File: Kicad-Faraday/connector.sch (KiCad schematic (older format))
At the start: 29 parts, among them P11 DNP, P12 DNP, P13 DNP, P14 DNP, P3 DNP, P4 DNP, P6 DNP, P7 DNP, P8 DNP, P9 DNP

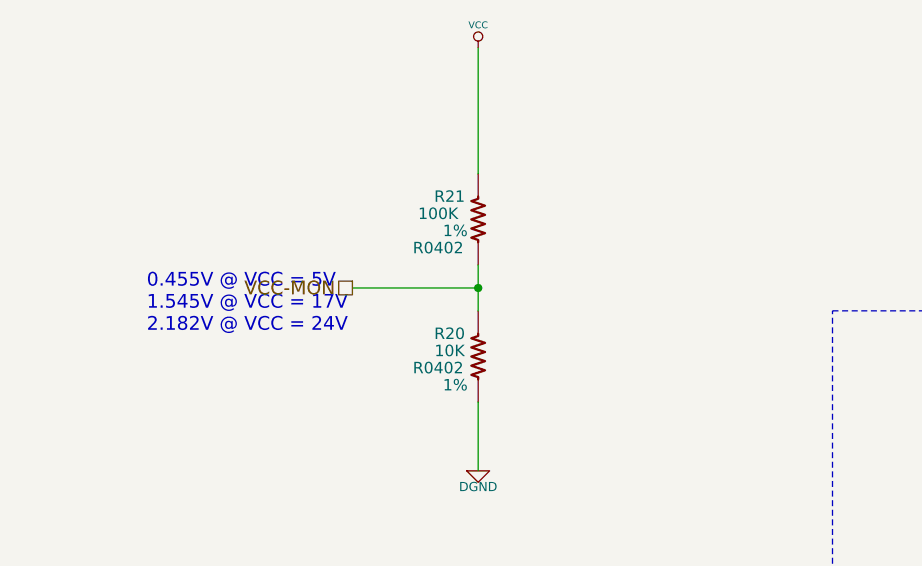
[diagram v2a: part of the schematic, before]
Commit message: Updated with ideal diode after realizing that the normal diodes have too large of a voltage drop... woops. Also added via fences back in.
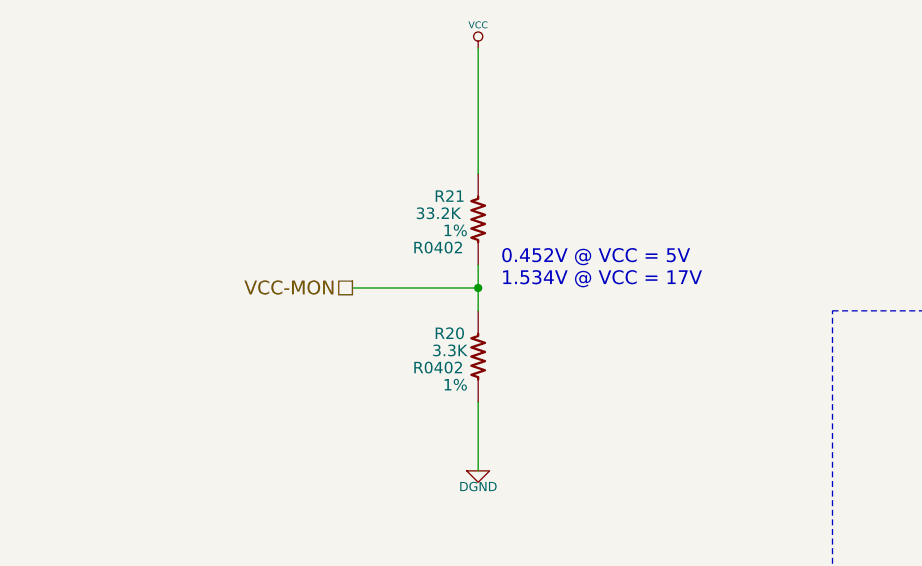
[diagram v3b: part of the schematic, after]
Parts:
- R20: value 10K -> 3.3K
- R21: value 100K -> 33.2K
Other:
- note added: "0.452V @ VCC = 5V\n1.534V @ VCC = 17V"
- note removed: "0.455V @ VCC = 5V\n1.545V @ VCC = 17V\n2.182V @ VCC = 24V"
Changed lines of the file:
@@
 Sheet 10 11
 Title "Faraday Wireless Node"
-Date "11 nov 2016"
+Date "13 nov 2016"
 Rev "C"
 Comp "FaradayRF"
@@
 Mounting Holes 125 mil
 $Comp
-L +3.3V #PWR090
+L +3.3V #PWR091
 U 1 1 54FD3F6B
 P 6000 5000
-F 0 "#PWR090" H 6000 4960 30  0001 C CNN
+F 0 "#PWR091" H 6000 4960 30  0001 C CNN
 F 1 "+3.3V" H 6000 5110 30  0000 C CNN
 F 2 "" H 6000 5000 60  0000 C CNN
@@
 $EndComp
 $Comp
-L VCC #PWR091
+L VCC #PWR092
 U 1 1 54FE705E
 P 6450 8900
-F 0 "#PWR091" H 6450 9000 30  0001 C CNN
+F 0 "#PWR092" H 6450 9000 30  0001 C CNN
 F 1 "VCC" H 6450 9000 30  0000 C CNN
 F 2 "" H 6450 8900 60  0000 C CNN
@@
 Ext. Power/MOSFET
 $Comp
-L DGND #PWR092
+L DGND #PWR093
 U 1 1 55A56688
 P 11550 3900
-F 0 "#PWR092" H 11550 3900 40  0001 C CNN
+F 0 "#PWR093" H 11550 3900 40  0001 C CNN
 F 1 "DGND" H 11550 3830 40  0000 C CNN
 F 2 "~" H 11550 3900 60  0000 C CNN
@@
 $EndComp
 $Comp
-L DGND #PWR093
+L DGND #PWR094
 U 1 1 55A56A07
 P 6200 4600
-F 0 "#PWR093" H 6200 4600 40  0001 C CNN
+F 0 "#PWR094" H 6200 4600 40  0001 C CNN
 F 1 "DGND" H 6200 4530 40  0000 C CNN
 F 2 "~" H 6200 4600 60  0000 C CNN
@@
 $EndComp
 $Comp
-L GNDPWR #PWR094
+L GNDPWR #PWR095
 U 1 1 55C2A828
 P 5750 7150
-F 0 "#PWR094" H 5750 7200 40  0001 C CNN
+F 0 "#PWR095" H 5750 7200 40  0001 C CNN
 F 1 "GNDPWR" H 5750 7070 40  0000 C CNN
 F 2 "" H 5750 7150 60  0000 C CNN
@@
 P 3050 2500
 F 0 "R21" H 2925 2600 50  0000 C CNN
-F 1 "100K" H 2875 2525 50  0000 C CNN
+F 1 "33.2K" H 2875 2525 50  0000 C CNN
 F 2 "R0402" H 2875 2375 50  0000 C CNN
 F 3 "" H 3050 2500 60  0000 C CNN
@@
 P 3050 3100
 F 0 "R20" H 2925 3200 50  0000 C CNN
-F 1 "10K" H 2925 3125 50  0000 C CNN
+F 1 "3.3K" H 2925 3125 50  0000 C CNN
 F 2 "R0402" H 2875 3050 50  0000 C CNN
 F 3 "" H 3050 3100 60  0000 C CNN
@@
 Text HLabel 2500 2800 0    60   UnSpc ~ 0
 VCC-MON
-Text Notes 1600 3000 0    60   ~ 0
-0.455V @ VCC = 5V\n1.545V @ VCC = 17V\n2.182V @ VCC = 24V
-$Comp
-L DGND #PWR095
+Text Notes 3150 2800 0    60   ~ 0
+0.452V @ VCC = 5V\n1.534V @ VCC = 17V
+$Comp
+L DGND #PWR096
 U 1 1 55DDCB2D
 P 3050 3600
-F 0 "#PWR095" H 3050 3600 40  0001 C CNN
+F 0 "#PWR096" H 3050 3600 40  0001 C CNN
 F 1 "DGND" H 3050 3530 40  0000 C CNN
 F 2 "~" H 3050 3600 60  0000 C CNN
@@
 	2100 9300 2700 9300
 $Comp
-L PWR_FLAG #FLG096
+L PWR_FLAG #FLG097
 U 1 1 578D1476
 P 6625 9550
-F 0 "#FLG096" H 6625 9645 30  0001 C CNN
+F 0 "#FLG097" H 6625 9645 30  0001 C CNN
 F 1 "PWR_FLAG" H 6625 9730 30  0000 C CNN
 F 2 "" H 6625 9550 60  0000 C CNN
@@
 $EndComp
 $Comp
-L DGND #PWR097
+L DGND #PWR098
 U 1 1 578D1483
 P 5950 9500
-F 0 "#PWR097" H 5950 9500 40  0001 C CNN
+F 0 "#PWR098" H 5950 9500 40  0001 C CNN
 F 1 "DGND" H 5950 9430 40  0000 C CNN
 F 2 "~" H 5950 9500 60  0000 C CNN
@@
 Place on bottom of PCB
 $Comp
-L VCC #PWR098
+L VCC #PWR099
 U 1 1 578D8DFD
 P 3050 1750
-F 0 "#PWR098" H 3050 1850 30  0001 C CNN
+F 0 "#PWR099" H 3050 1850 30  0001 C CNN
 F 1 "VCC" H 3050 1850 30  0000 C CNN
 F 2 "" H 3050 1750 60  0000 C CNN
@@
 $EndComp
 $Comp
-L VCC #PWR099
+L VCC #PWR0100
 U 1 1 578D92A7
 P 6000 5400
-F 0 "#PWR099" H 6000 5500 30  0001 C CNN
+F 0 "#PWR0100" H 6000 5500 30  0001 C CNN
 F 1 "VCC" H 6000 5500 30  0000 C CNN
 F 2 "" H 6000 5400 60  0000 C CNN
@@
 $EndComp
 $Comp
-L PWR_FLAG #FLG0100
+L PWR_FLAG #FLG0101
 U 1 1 578DD49D
 P 6025 9450
-F 0 "#FLG0100" H 6025 9545 30  0001 C CNN
+F 0 "#FLG0101" H 6025 9545 30  0001 C CNN
 F 1 "PWR_FLAG" H 6025 9630 30  0000 C CNN
 F 2 "" H 6025 9450 60  0000 C CNN
@@
 $EndComp
 $Comp
-L DGND #PWR0101
+L DGND #PWR0102
 U 1 1 579B84BD
 P 7375 9600
-F 0 "#PWR0101" H 7375 9600 40  0001 C CNN
+F 0 "#PWR0102" H 7375 9600 40  0001 C CNN
 F 1 "DGND" H 7375 9530 40  0000 C CNN
 F 2 "~" H 7375 9600 60  0000 C CNN
@@
 	6450 8950 5850 8950
 $Comp
-L VCC #PWR0102
+L VCC #PWR0103
 U 1 1 579FA7FA
 P 6450 9575
-F 0 "#PWR0102" H 6450 9675 30  0001 C CNN
+F 0 "#PWR0103" H 6450 9675 30  0001 C CNN
 F 1 "VCC" H 6450 9675 30  0000 C CNN
 F 2 "" H 6450 9575 60  0000 C CNN

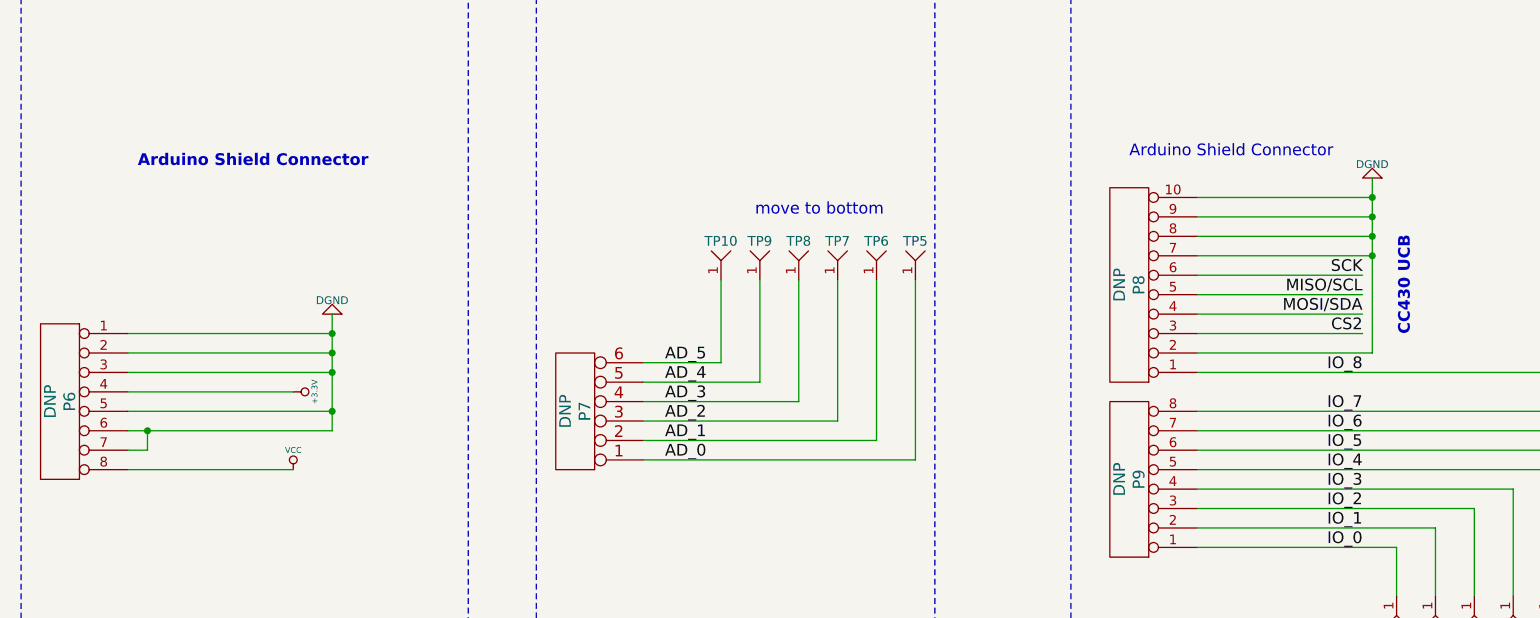
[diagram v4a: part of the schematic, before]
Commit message: Cleaned up a few connections on the schematic to make sure wire junctions were used. Also added a few notes such as LED color. Output new PDF of Schematics and updated Rev to Rev D1 for PCB:NG
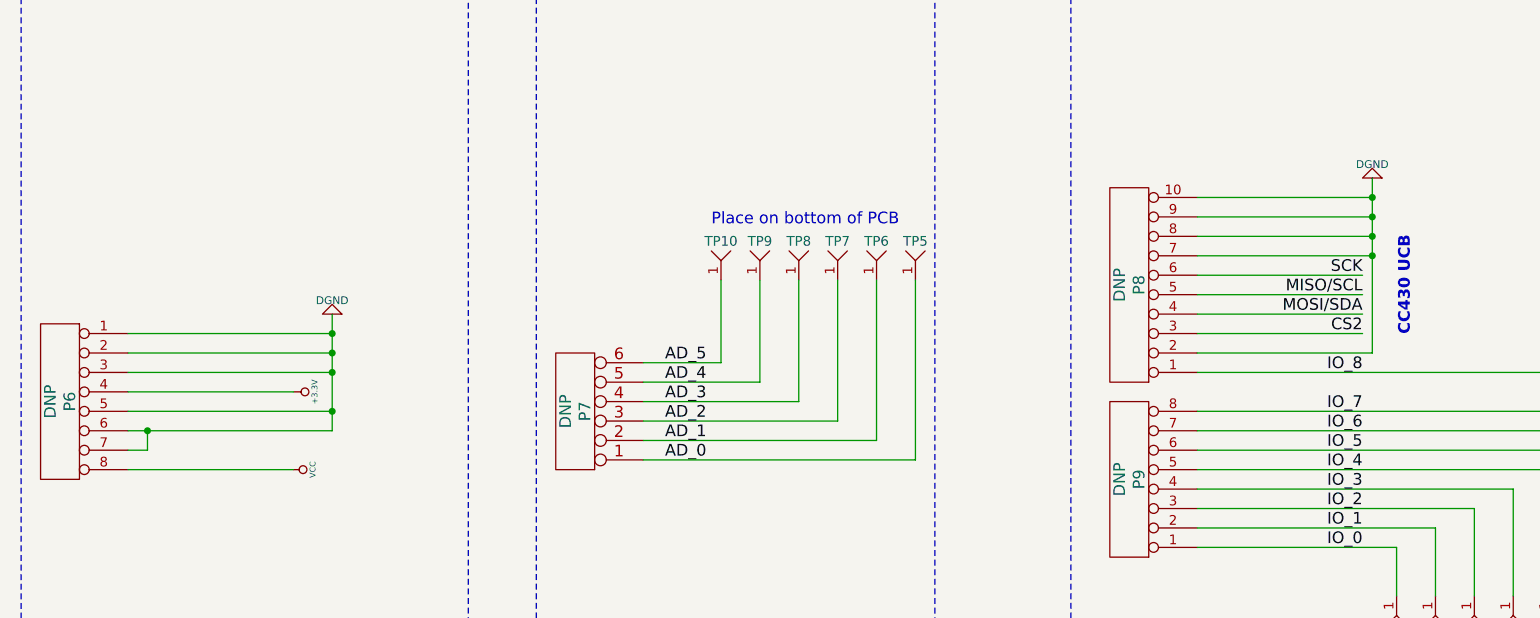
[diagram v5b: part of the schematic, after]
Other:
- note removed: "Arduino Shield Connector"
- note removed: "move to bottom"
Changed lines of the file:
@@
 Sheet 10 11
 Title "Faraday Wireless Node"
-Date "14 nov 2016"
-Rev "C"
+Date "15 nov 2016"
+Rev "D1"
 Comp "FaradayRF"
 Comment1 "www.FaradayRF.com"
@@
 Text Label 2700 9500 2    60   ~ 0
 CS2
-Text Notes 5200 3850 0    60   ~ 12
-Arduino Shield Connector
-Text Notes 10300 3800 0    60   ~ 0
-Arduino Shield Connector
 $Sheet
 S 11950 8550 950  350
@@
 Wire Wire Line
 	5850 9600 7075 9600
-Text Notes 8375 4100 0    60   ~ 0
-move to bottom
 $Comp
 L TEST-POINT TP16
@@
 F 3 "" H 6000 5400 60  0000 C CNN
 	1    6000 5400
-	1    0    0    -1
+	0    1    1    0
 $EndComp
 $Comp
@@
 Text Notes 4200 9550 0    60   ~ 0
 Molex 2.54mm Pitch
+Text Notes 8150 4150 0    60   ~ 0
+Place on bottom of PCB
 $EndSCHEMATC

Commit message: Exported new pick and place file
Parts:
- P3, P4: value DNP -> 0022232021
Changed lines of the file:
@@
 Sheet 10 11
 Title "Faraday Wireless Node"
-Date "16 nov 2016"
-Rev "D1"
+Date "18 nov 2016"
+Rev "D"
 Comp "FaradayRF"
 Comment1 "www.FaradayRF.com"
@@
 P 5500 8850
 F 0 "P3" V 5450 8850 40  0000 C CNN
-F 1 "DNP" V 5550 8850 40  0001 C CNN
+F 1 "0022232021" V 5550 8850 40  0001 C CNN
 F 2 "0022232021" H 5500 9050 60  0000 C CNN
 F 3 "" H 5500 8850 60  0000 C CNN
@@
 P 5500 9500
 F 0 "P4" V 5450 9500 40  0000 C CNN
-F 1 "DNP" V 5550 9500 40  0001 C CNN
+F 1 "0022232021" V 5550 9500 40  0001 C CNN
 F 2 "0022232021" H 5500 9750 60  0000 C CNN
 F 3 "" H 5500 9500 60  0000 C CNN
